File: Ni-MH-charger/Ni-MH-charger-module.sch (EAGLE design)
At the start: 12 parts

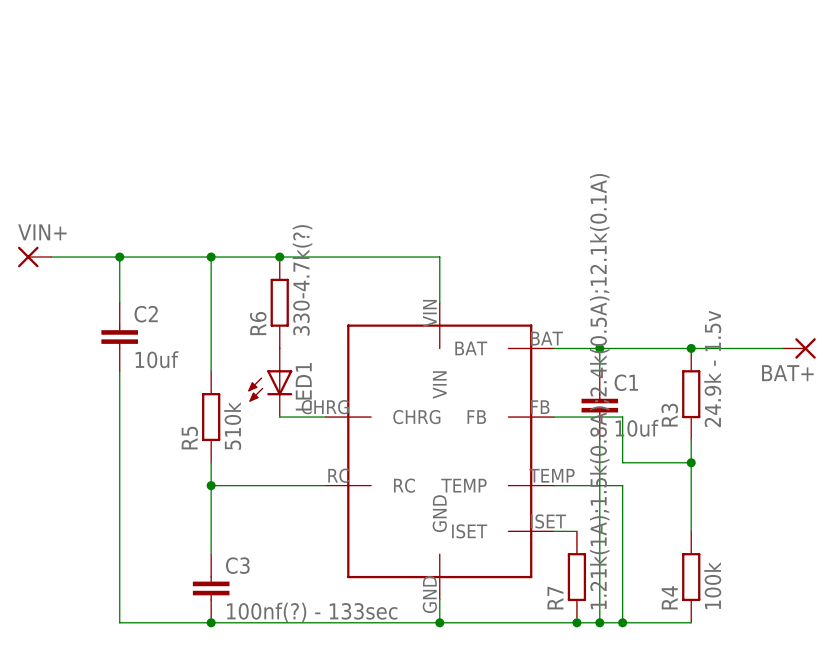
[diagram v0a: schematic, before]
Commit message: Ni-MH-charger updated
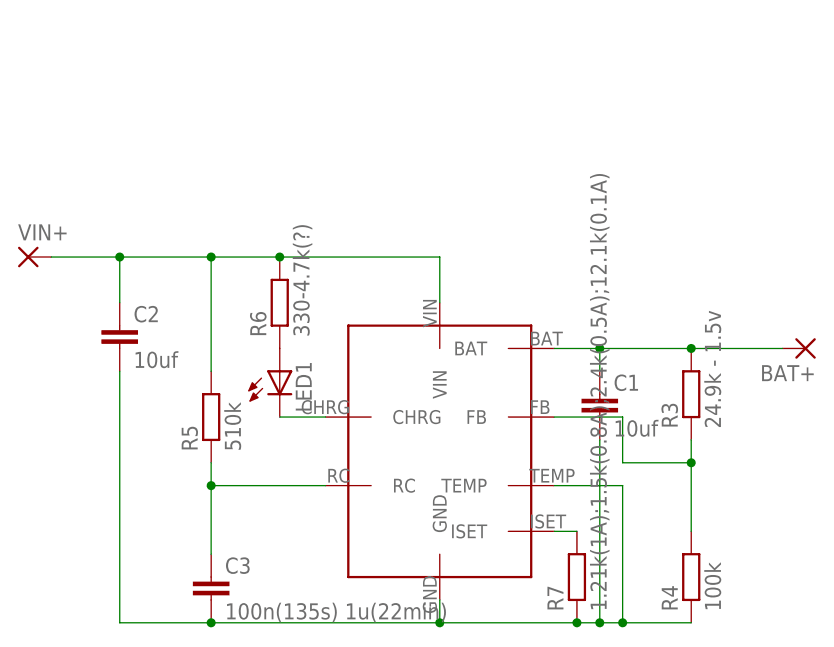
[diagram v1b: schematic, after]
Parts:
- C3: value 100nf(?) - 133sec -> 100n(135s) 1u(22min)
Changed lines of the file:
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@@
 <grid distance="0.1" unitdist="inch" unit="inch" style="lines" multiple="1" display="no" altdistance="0.01" altunitdist="inch" altunit="inch"/>
 <layers>
-<layer number="1" name="Top" color="4" fill="1" visible="yes" active="no"/>
-<layer number="16" name="Bottom" color="1" fill="1" visible="yes" active="no"/>
-<layer number="17" name="Pads" color="2" fill="1" visible="yes" active="no"/>
-<layer number="18" name="Vias" color="2" fill="1" visible="yes" active="no"/>
-<layer number="19" name="Unrouted" color="6" fill="1" visible="yes" active="no"/>
-<layer number="20" name="Dimension" color="24" fill="1" visible="yes" active="no"/>
-<layer number="21" name="tPlace" color="7" fill="1" visible="yes" active="no"/>
-<layer number="22" name="bPlace" color="7" fill="1" visible="yes" active="no"/>
-<layer number="23" name="tOrigins" color="15" fill="1" visible="yes" active="no"/>
-<layer number="24" name="bOrigins" color="15" fill="1" visible="yes" active="no"/>
-<layer number="25" name="tNames" color="7" fill="1" visible="yes" active="no"/>
-<layer number="26" name="bNames" color="7" fill="1" visible="yes" active="no"/>
-<layer number="27" name="tValues" color="7" fill="1" visible="yes" active="no"/>
-<layer number="28" name="bValues" color="7" fill="1" visible="yes" active="no"/>
+<layer number="1" name="Top" color="4" fill="1" visible="no" active="no"/>
+<layer number="16" name="Bottom" color="1" fill="1" visible="no" active="no"/>
+<layer number="17" name="Pads" color="2" fill="1" visible="no" active="no"/>
+<layer number="18" name="Vias" color="2" fill="1" visible="no" active="no"/>
+<layer number="19" name="Unrouted" color="6" fill="1" visible="no" active="no"/>
+<layer number="20" name="Dimension" color="24" fill="1" visible="no" active="no"/>
+<layer number="21" name="tPlace" color="7" fill="1" visible="no" active="no"/>
+<layer number="22" name="bPlace" color="7" fill="1" visible="no" active="no"/>
+<layer number="23" name="tOrigins" color="15" fill="1" visible="no" active="no"/>
+<layer number="24" name="bOrigins" color="15" fill="1" visible="no" active="no"/>
+<layer number="25" name="tNames" color="7" fill="1" visible="no" active="no"/>
+<layer number="26" name="bNames" color="7" fill="1" visible="no" active="no"/>
+<layer number="27" name="tValues" color="7" fill="1" visible="no" active="no"/>
+<layer number="28" name="bValues" color="7" fill="1" visible="no" active="no"/>
 <layer number="29" name="tStop" color="7" fill="3" visible="no" active="no"/>
 <layer number="30" name="bStop" color="7" fill="6" visible="no" active="no"/>
@@
 <layer number="35" name="tGlue" color="7" fill="4" visible="no" active="no"/>
 <layer number="36" name="bGlue" color="7" fill="5" visible="no" active="no"/>
-<layer number="37" name="tTest" color="7" fill="1" visible="yes" active="no"/>
-<layer number="38" name="bTest" color="7" fill="1" visible="yes" active="no"/>
+<layer number="37" name="tTest" color="7" fill="1" visible="no" active="no"/>
+<layer number="38" name="bTest" color="7" fill="1" visible="no" active="no"/>
 <layer number="39" name="tKeepout" color="4" fill="11" visible="no" active="no"/>
 <layer number="40" name="bKeepout" color="1" fill="11" visible="no" active="no"/>
@@
 <layer number="44" name="Drills" color="7" fill="1" visible="no" active="no"/>
 <layer number="45" name="Holes" color="7" fill="1" visible="no" active="no"/>
-<layer number="46" name="Milling" color="3" fill="1" visible="yes" active="no"/>
-<layer number="47" name="Measures" color="7" fill="1" visible="yes" active="no"/>
-<layer number="48" name="Document" color="7" fill="1" visible="yes" active="no"/>
-<layer number="49" name="Reference" color="7" fill="1" visible="yes" active="no"/>
-<layer number="50" name="dxf" color="7" fill="1" visible="yes" active="no"/>
-<layer number="51" name="tDocu" color="7" fill="1" visible="yes" active="no"/>
-<layer number="52" name="bDocu" color="7" fill="1" visible="yes" active="no"/>
-<layer number="53" name="tGND_GNDA" color="7" fill="9" visible="yes" active="no"/>
-<layer number="54" name="bGND_GNDA" color="1" fill="9" visible="yes" active="no"/>
-<layer number="56" name="wert" color="7" fill="1" visible="yes" active="no"/>
-<layer number="57" name="tCAD" color="7" fill="1" visible="yes" active="no"/>
-<layer number="59" name="tCarbon" color="7" fill="1" visible="yes" active="no"/>
-<layer number="60" name="bCarbon" color="7" fill="1" visible="yes" active="no"/>
+<layer number="46" name="Milling" color="3" fill="1" visible="no" active="no"/>
+<layer number="47" name="Measures" color="7" fill="1" visible="no" active="no"/>
+<layer number="48" name="Document" color="7" fill="1" visible="no" active="no"/>
+<layer number="49" name="Reference" color="7" fill="1" visible="no" active="no"/>
+<layer number="50" name="dxf" color="7" fill="1" visible="no" active="no"/>
+<layer number="51" name="tDocu" color="7" fill="1" visible="no" active="no"/>
+<layer number="52" name="bDocu" color="7" fill="1" visible="no" active="no"/>
+<layer number="53" name="tGND_GNDA" color="7" fill="9" visible="no" active="no"/>
+<layer number="54" name="bGND_GNDA" color="1" fill="9" visible="no" active="no"/>
+<layer number="56" name="wert" color="7" fill="1" visible="no" active="no"/>
+<layer number="57" name="tCAD" color="7" fill="1" visible="no" active="no"/>
+<layer number="59" name="tCarbon" color="7" fill="1" visible="no" active="no"/>
+<layer number="60" name="bCarbon" color="7" fill="1" visible="no" active="no"/>
 <layer number="90" name="Modules" color="5" fill="1" visible="yes" active="yes"/>
 <layer number="91" name="Nets" color="2" fill="1" visible="yes" active="yes"/>
@@
 <part name="C2" library="resistor" library_urn="urn:adsk.eagle:library:348" deviceset="C-EU" device="C0805" package3d_urn="urn:adsk.eagle:package:26137/1" value="10uf"/>
 <part name="BAT+" library="wirepad" library_urn="urn:adsk.eagle:library:412" deviceset="SMD5" device="" package3d_urn="urn:adsk.eagle:package:30841/1"/>
-<part name="C3" library="resistor" library_urn="urn:adsk.eagle:library:348" deviceset="C-EU" device="C0805" package3d_urn="urn:adsk.eagle:package:26137/1" value="100nf(?) - 133sec"/>
+<part name="C3" library="resistor" library_urn="urn:adsk.eagle:library:348" deviceset="C-EU" device="C0805" package3d_urn="urn:adsk.eagle:package:26137/1" value="100n(135s) 1u(22min)"/>
 <part name="VIN+" library="wirepad" library_urn="urn:adsk.eagle:library:412" deviceset="SMD5" device="" package3d_urn="urn:adsk.eagle:package:30841/1"/>
 <part name="LED1" library="adafruit" deviceset="LED" device="CHIPLED_0805"/>

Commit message: Ni-MH-charger updates
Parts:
- C3: value 100n(135s) 1u(22min) -> 10uf
- R5: value 510k -> 750k
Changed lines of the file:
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@@
 <part name="R3" library="resistor" library_urn="urn:adsk.eagle:library:348" deviceset="R-EU_" device="R0805" package3d_urn="urn:adsk.eagle:package:26059/1" value="24.9k - 1.5v"/>
 <part name="R4" library="resistor" library_urn="urn:adsk.eagle:library:348" deviceset="R-EU_" device="R0805" package3d_urn="urn:adsk.eagle:package:26059/1" value="100k"/>
-<part name="R5" library="resistor" library_urn="urn:adsk.eagle:library:348" deviceset="R-EU_" device="R0805" package3d_urn="urn:adsk.eagle:package:26059/1" value="510k"/>
+<part name="R5" library="resistor" library_urn="urn:adsk.eagle:library:348" deviceset="R-EU_" device="R0805" package3d_urn="urn:adsk.eagle:package:26059/1" value="750k"/>
 <part name="R6" library="resistor" library_urn="urn:adsk.eagle:library:348" deviceset="R-EU_" device="R0805" package3d_urn="urn:adsk.eagle:package:26059/1" value="330-4.7k(?)"/>
 <part name="R7" library="resistor" library_urn="urn:adsk.eagle:library:348" deviceset="R-EU_" device="R0805" package3d_urn="urn:adsk.eagle:package:26059/1" value="1.21k(1A);1.5k(0.8A);2.4k(0.5A);12.1k(0.1A)"/>
@@
 <part name="C2" library="resistor" library_urn="urn:adsk.eagle:library:348" deviceset="C-EU" device="C0805" package3d_urn="urn:adsk.eagle:package:26137/1" value="10uf"/>
 <part name="BAT+" library="wirepad" library_urn="urn:adsk.eagle:library:412" deviceset="SMD5" device="" package3d_urn="urn:adsk.eagle:package:30841/1"/>
-<part name="C3" library="resistor" library_urn="urn:adsk.eagle:library:348" deviceset="C-EU" device="C0805" package3d_urn="urn:adsk.eagle:package:26137/1" value="100n(135s) 1u(22min)"/>
+<part name="C3" library="resistor" library_urn="urn:adsk.eagle:library:348" deviceset="C-EU" device="C0805" package3d_urn="urn:adsk.eagle:package:26137/1" value="10uf"/>
 <part name="VIN+" library="wirepad" library_urn="urn:adsk.eagle:library:412" deviceset="SMD5" device="" package3d_urn="urn:adsk.eagle:package:30841/1"/>
 <part name="LED1" library="adafruit" deviceset="LED" device="CHIPLED_0805"/>
